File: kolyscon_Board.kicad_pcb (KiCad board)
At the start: 2 copper layers, 88 x 68.5 mm, 48 parts, among them J1 Conn_01x04, U1 74HC595, U2 74HC595

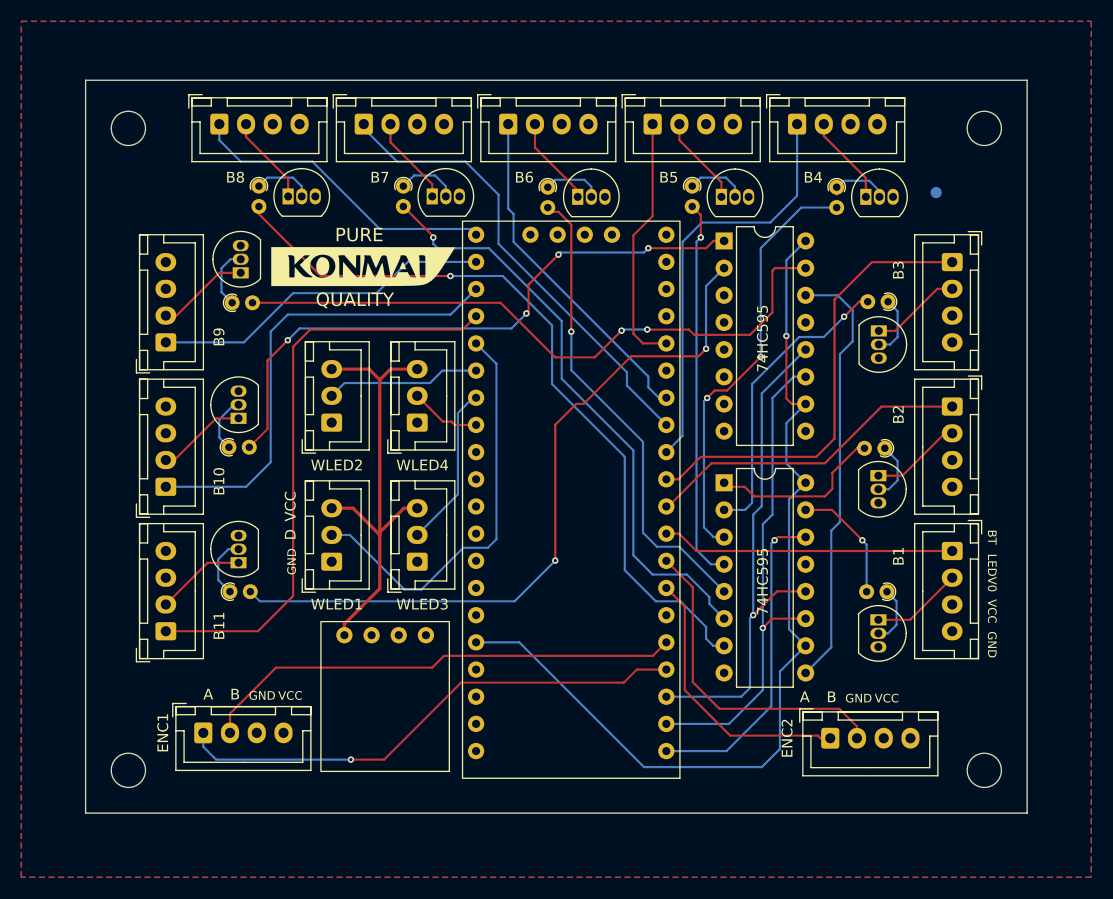
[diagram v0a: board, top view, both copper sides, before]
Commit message: Trace cleanups
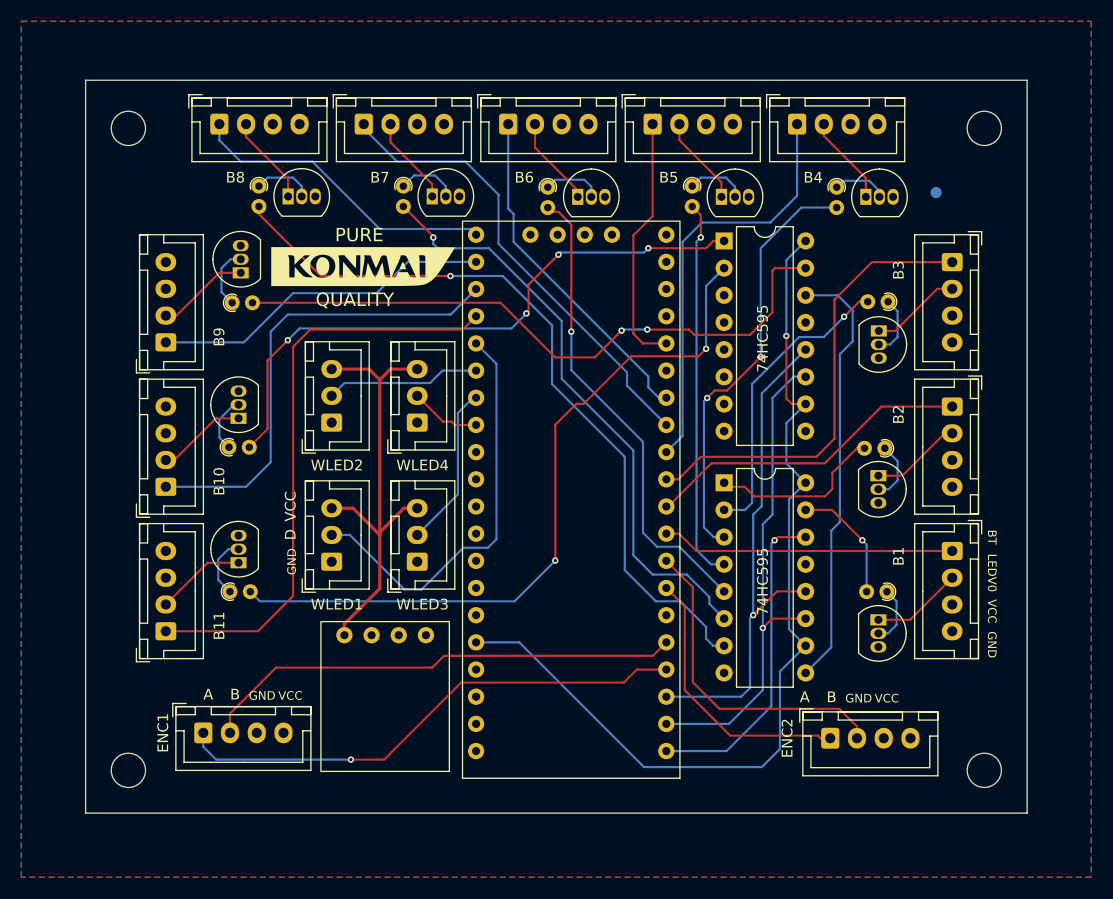
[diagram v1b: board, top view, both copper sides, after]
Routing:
- net /ENC_1_A: track 49.2 -> 48.6 mm
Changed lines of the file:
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@@
-	)
-	(segment
-		(start 77 126.5)
-		(end 77 127.1)
-		(width 0.2)
-		(layer "F.Cu")
-		(net 16)
 	)
 	(segment
@@
 	)
 	(segment
-		(start 78 128.8)
+		(start 77 127.8)
 		(end 78.2 129)
-		(width 0.2)
-		(layer "B.Cu")
-		(net 16)
-	)
-	(segment
-		(start 77 127.8)
-		(end 78 128.8)
 		(width 0.2)
 		(layer "B.Cu")
@@
 	)
 	(segment
-		(start 136.2 75.9)
-		(end 136.2 76.2)
-		(width 0.2)
-		(layer "F.Cu")
-		(net 77)
-	)
-	(segment

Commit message: Small text changes
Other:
- board text added: "Free design & software"
- board text removed: "Free design and software"

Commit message: 1.2 version bump -Slightly better 5v and gnd planes
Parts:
- moved ENC2 1.20 mm to (134.4, 127.0)
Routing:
- net /ENC_2_B: track 30.5 -> 28.8 mm
- net /ENC_2_A: track 25.7 -> 24.9 mm
- net /ENC_1_B: vias 0 -> 1
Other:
- board text added: "Kolyscon_Board V1.2"
- board text removed: "Kolyscon_Board V1.1"
